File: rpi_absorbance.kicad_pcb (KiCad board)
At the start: 2 copper layers, 33 parts, among them CON1 BARREL_JACK, P1 CONN_02X04, P2 CONN_01X02, P3 RPI_HEADER, P4 STEPPER_CONN, P5 CONN_02X05, Q1 ZTX692B, U1 R-78B5.0-1.5L, U2 MUN5216DW1T1G, U3 DRV8825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

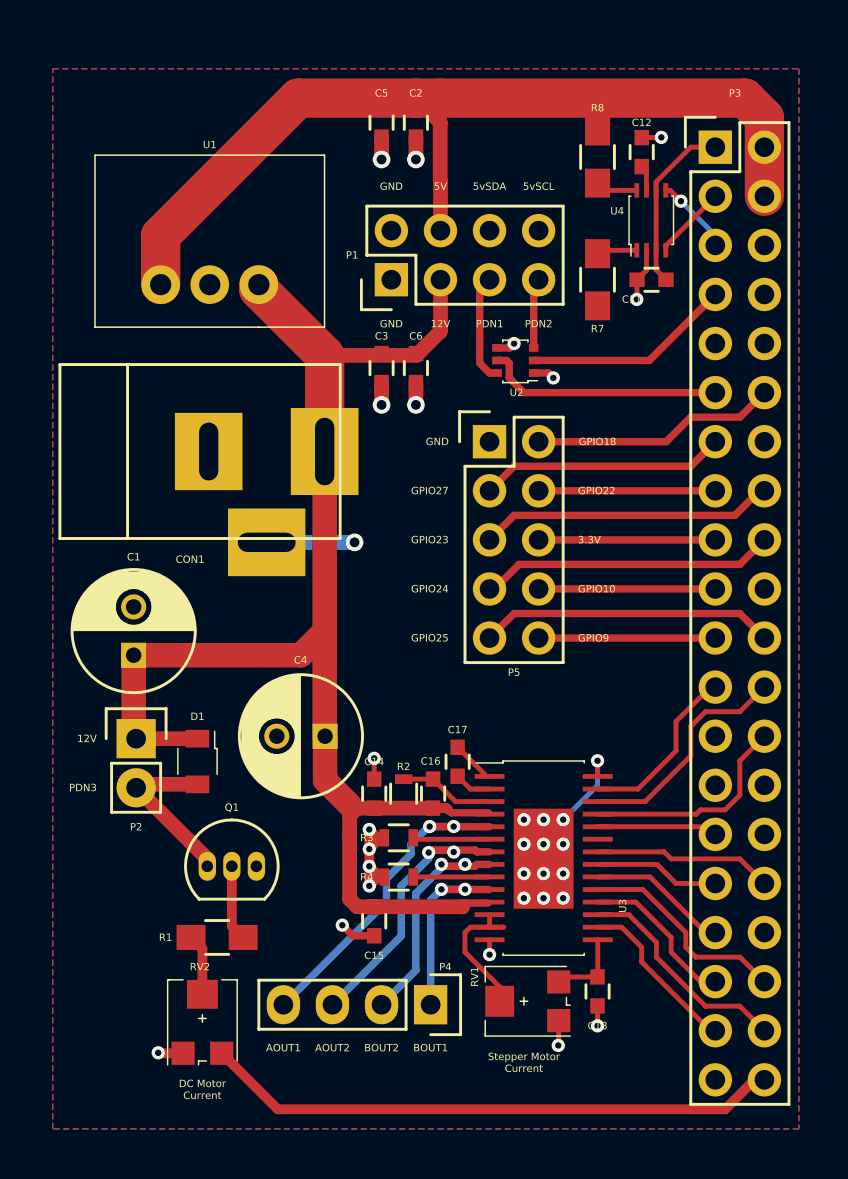
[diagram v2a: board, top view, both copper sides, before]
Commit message: Add missing connections
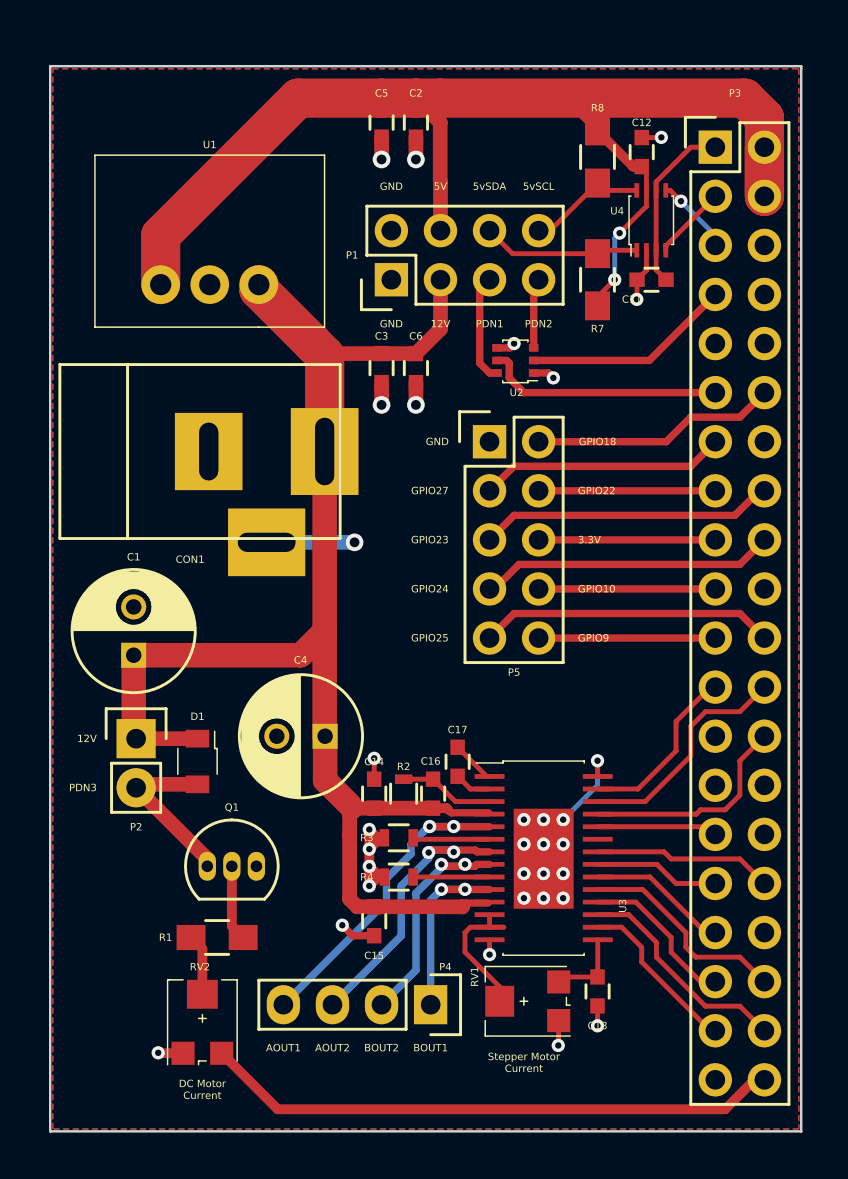
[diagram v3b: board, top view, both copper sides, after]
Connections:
- P3 pad 17: +3V3 -> /3.3v
- P5 pad 6: +3V3 -> /3.3v
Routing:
- net +5V: track 49.9 -> 73.7 mm, vias 0 -> 2
- net /3.3v: track 0.00 -> 9.14 mm
- net +3V3: track 18.2 -> 9.08 mm
- net /5vSDA: track 2.46 -> 8.54 mm
- net /5vSCL: track 1.66 -> 5.72 mm
- net +12V: track 75.4 -> 78.3 mm
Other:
- board outline added: 38.9 x 55.1 mm
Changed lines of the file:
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@@
 (kicad_pcb (version 4) (host pcbnew 4.0.2-4+6225~38~ubuntu14.04.1-stable)
   (general
-    (links 111)
-    (no_connects 43)
-    (area 145.288 90.932 184.055401 145.796001)
+    (links 110)
+    (no_connects 0)
+    (area 0 0 0 0)
     (thickness 1.6)
-    (drawings 26)
-    (tracks 357)
+    (drawings 31)
+    (tracks 383)
     (zones 0)
     (modules 33)
-    (nets 47)
+    (nets 48)
   )
   (page A4)
@@
   )
   (setup
-    (last_trace_width 2.032)
+    (last_trace_width 0.381)
     (user_trace_width 0.254)
     (user_trace_width 0.381)
@@
   (net 45 /GPIO27)
   (net 46 /GPIO22)
+  (net 47 /3.3v)
   (net_class Default "This is the default net class."
     (clearance 0.1524)
@@
     (add_net +3V3)
     (add_net +5V)
+    (add_net /3.3v)
     (add_net /3.3vSCL)
     (add_net /3.3vSDA)
@@
       (net 41 /GPIO23))
     (pad 17 thru_hole oval (at 0 20.32) (size 1.7272 1.7272) (drill 1.016) (layers *.Cu *.Mask F.SilkS)
-      (net 4 +3V3))
+      (net 47 /3.3v))
     (pad 18 thru_hole oval (at 2.54 20.32) (size 1.7272 1.7272) (drill 1.016) (layers *.Cu *.Mask F.SilkS)
       (net 42 /GPIO24))
@@
       (net 41 /GPIO23))
     (pad 6 thru_hole oval (at 2.54 5.08) (size 1.7272 1.7272) (drill 1.016) (layers *.Cu *.Mask F.SilkS)
-      (net 4 +3V3))
+      (net 47 /3.3v))
     (pad 7 thru_hole oval (at 0 7.62) (size 1.7272 1.7272) (drill 1.016) (layers *.Cu *.Mask F.SilkS)
       (net 42 /GPIO24))
@@
     )
   )
+  (gr_line (start 184.023 90.805) (end 184.023 90.932) (angle 90) (layer Edge.Cuts) (width 0.127))
+  (gr_line (start 145.161 90.805) (end 184.023 90.805) (angle 90) (layer Edge.Cuts) (width 0.127))
+  (gr_line (start 145.161 145.923) (end 145.161 90.805) (angle 90) (layer Edge.Cuts) (width 0.127))
+  (gr_line (start 184.023 145.923) (end 145.161 145.923) (angle 90) (layer Edge.Cuts) (width 0.127))
+  (gr_line (start 184.023 90.932) (end 184.023 145.923) (angle 90) (layer Edge.Cuts) (width 0.127))
   (gr_text PDN3 (at 147.574 128.143) (layer F.SilkS)
     (effects (font (size 0.381 0.381) (thickness 0.0762)) (justify right))
@@
     (effects (font (size 0.381 0.381) (thickness 0.0762)))
   )
+  (segment (start 161.925 129.1978) (end 163.449 129.1978) (width 0.381) (layer F.Cu) (net 1))
+  (segment (start 162.306 105.676) (end 159.27 105.676) (width 0.762) (layer F.Cu) (net 1))
+  (segment (start 158.75 105.918) (end 158.75 105.156) (width 0.762) (layer F.Cu) (net 1))
+  (segment (start 159.028 105.918) (end 158.75 105.918) (width 0.762) (layer F.Cu) (net 1))
+  (segment (start 159.27 105.676) (end 159.028 105.918) (width 0.762) (layer F.Cu) (net 1))
+  (segment (start 164.084 105.676) (end 162.306 105.676) (width 0.762) (layer F.Cu) (net 1))
+  (segment (start 165.354 101.854) (end 165.354 104.406) (width 0.762) (layer F.Cu) (net 1))
+  (segment (start 165.354 104.406) (end 164.084 105.676) (width 0.762) (layer F.Cu) (net 1))
   (segment (start 155.956 102.108) (end 155.956 102.362) (width 2.032) (layer F.Cu) (net 1))
-  (segment (start 155.956 102.362) (end 159.36214 105.76814) (width 2.032) (layer F.Cu) (net 1))
-  (segment (start 165.342 104.394) (end 165.342 104.533) (width 0.762) (layer F.Cu) (net 1))
-  (segment (start 165.342 104.533) (end 164.10686 105.76814) (width 0.762) (layer F.Cu) (net 1))
-  (segment (start 164.10686 105.76814) (end 159.36214 105.76814) (width 0.762) (layer F.Cu) (net 1))
-  (segment (start 165.354 101.854) (end 165.354 104.382) (width 0.762) (layer F.Cu) (net 1))
-  (segment (start 165.354 104.382) (end 165.342 104.394) (width 0.762) (layer F.Cu) (net 1))
+  (segment (start 155.956 102.362) (end 158.75 105.156) (width 2.032) (layer F.Cu) (net 1))
+  (segment (start 158.75 105.156) (end 159.36214 105.76814) (width 2.032) (layer F.Cu) (net 1))
+  (segment (start 159.36214 110.744) (end 159.36214 105.76814) (width 2.032) (layer F.Cu) (net 1))
   (segment (start 152.781 125.603) (end 149.606 125.603) (width 0.762) (layer F.Cu) (net 1))
   (segment (start 149.479 121.285) (end 149.479 125.476) (width 1.27) (layer F.Cu) (net 1))
@@
   (segment (start 159.385 110.76686) (end 159.36214 110.744) (width 1.27) (layer F.Cu) (net 1))
   (segment (start 159.385 110.76686) (end 159.36214 110.744) (width 0.762) (layer F.Cu) (net 1))
-  (segment (start 159.36214 110.744) (end 159.36214 105.76814) (width 2.032) (layer F.Cu) (net 1))
   (segment (start 167.8178 134.112) (end 166.6734 134.112) (width 0.381) (layer F.Cu) (net 1))
   (segment (start 166.6734 134.112) (end 166.4836 134.3018) (width 0.381) (layer F.Cu) (net 1))
@@
   (segment (start 171.7035 131.8138) (end 170.694 131.8138) (width 0.254) (layer F.Cu) (net 2))
   (segment (start 170.688 133.9088) (end 170.694 133.9028) (width 0.254) (layer F.Cu) (net 2))
+  (segment (start 182.118 94.996) (end 182.118 97.536) (width 2.032) (layer F.Cu) (net 3))
+  (segment (start 176.014 97.23) (end 176.014 98.052) (width 0.254) (layer F.Cu) (net 3))
+  (segment (start 174.371 101.854) (end 173.482 102.743) (width 0.254) (layer F.Cu) (net 3))
+  (via (at 174.371 101.854) (size 0.6858) (drill 0.3302) (layers F.Cu B.Cu) (net 3))
+  (segment (start 174.371 99.695) (end 174.371 101.854) (width 0.254) (layer B.Cu) (net 3))
+  (segment (start 174.625 99.441) (end 174.371 99.695) (width 0.254) (layer B.Cu) (net 3))
+  (via (at 174.625 99.441) (size 0.6858) (drill 0.3302) (layers F.Cu B.Cu) (net 3))
+  (segment (start 176.014 98.052) (end 174.625 99.441) (width 0.254) (layer F.Cu) (net 3))
+  (segment (start 173.482 102.743) (end 173.482 103.204) (width 0.254) (layer F.Cu) (net 3))
+  (segment (start 175.328 96) (end 173.482 94.154) (width 0.508) (layer F.Cu) (net 3))
+  (segment (start 175.768 96) (end 175.328 96) (width 0.508) (layer F.Cu) (net 3))
+  (segment (start 164.084 92.976) (end 172.304 92.976) (width 0.381) (layer F.Cu) (net 3))
+  (segment (start 172.304 92.976) (end 173.482 94.154) (width 0.381) (layer F.Cu) (net 3))
+  (segment (start 164.084 92.976) (end 164.084 92.456) (width 0.381) (layer F.Cu) (net 3))
+  (segment (start 162.306 92.976) (end 162.306 92.456) (width 0.381) (layer F.Cu) (net 3))
+  (segment (start 162.306 92.456) (end 162.306 92.329) (width 0.381) (layer F.Cu) (net 3))
+  (segment (start 162.306 92.329) (end 162.306 92.456) (width 0.381) (layer F.Cu) (net 3))
   (segment (start 150.876 102.108) (end 150.876 99.568) (width 2.032) (layer F.Cu) (net 3))
-  (segment (start 157.988 92.456) (end 164.084 92.456) (width 2.032) (layer F.Cu) (net 3))
+  (segment (start 157.988 92.456) (end 162.306 92.456) (width 2.032) (layer F.Cu) (net 3))
+  (segment (start 162.306 92.456) (end 164.084 92.456) (width 2.032) (layer F.Cu) (net 3))
   (segment (start 150.876 99.568) (end 157.988 92.456) (width 2.032) (layer F.Cu) (net 3))
   (segment (start 165.342 96.774) (end 165.342 93.714) (width 0.762) (layer F.Cu) (net 3))
@@
   (segment (start 176.014 96.246) (end 175.768 96) (width 0.254) (layer F.Cu) (net 3))
   (segment (start 176.014 95.762) (end 176.01 95.758) (width 0.254) (layer F.Cu) (net 3))
-  (segment (start 179.578 115.316) (end 170.434 115.316) (width 0.381) (layer F.Cu) (net 4))
   (segment (start 176.514 97.23) (end 176.514 100.33) (width 0.254) (layer F.Cu) (net 4))
   (segment (start 176.514 100.33) (end 176.514 101.342) (width 0.254) (layer F.Cu) (net 4))
@@
   (segment (start 173.494 136.0088) (end 173.494 137.922) (width 0.254) (layer F.Cu) (net 8))
   (segment (start 173.494 137.922) (end 173.482 137.934) (width 0.254) (layer F.Cu) (net 8))
+  (segment (start 173.482 100.504) (end 169.084 100.504) (width 0.254) (layer F.Cu) (net 9))
+  (segment (start 169.084 100.504) (end 167.894 99.314) (width 0.254) (layer F.Cu) (net 9))
   (segment (start 175.514 100.33) (end 173.656 100.33) (width 0.254) (layer F.Cu) (net 9))
   (segment (start 173.656 100.33) (end 173.402 100.584) (width 0.254) (layer F.Cu) (net 9))
   (segment (start 173.656 100.33) (end 173.482 100.504) (width 0.254) (layer F.Cu) (net 9))
+  (segment (start 170.434 99.314) (end 171.022 99.314) (width 0.254) (layer F.Cu) (net 10))
+  (segment (start 171.022 99.314) (end 173.482 96.854) (width 0.254) (layer F.Cu) (net 10))
   (segment (start 175.514 97.23) (end 173.858 97.23) (width 0.254) (layer F.Cu) (net 10))
   (segment (start 177.014 100.33) (end 177.014 100.1) (width 0.254) (layer F.Cu) (net 11))
@@
   (segment (start 178.308 111.506) (end 169.164 111.506) (width 0.381) (layer F.Cu) (net 45))
   (segment (start 179.578 112.776) (end 170.434 112.776) (width 0.381) (layer F.Cu) (net 46))
+  (segment (start 179.578 115.316) (end 170.434 115.316) (width 0.381) (layer F.Cu) (net 47))
   (zone (net 2) (net_name GND) (layer F.Cu) (hatch edge 0.508)
     (connect_pads yes (clearance 0.254))
     (min_thickness 0.254)
-    (fill (arc_segments 16) (thermal_gap 0.508) (thermal_bridge_width 0.508))
+    (fill yes (arc_segments 16) (thermal_gap 0.508) (thermal_bridge_width 0.508))
     (polygon
       (pts
@@
     (connect_pads yes (clearance 0.254))
     (min_thickness 0.254)
-    (fill (arc_segments 16) (thermal_gap 0.508) (thermal_bridge_width 0.508))
+    (fill yes (arc_segments 16) (thermal_gap 0.508) (thermal_bridge_width 0.508))
     (polygon
       (pts

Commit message: Replace power input footprint
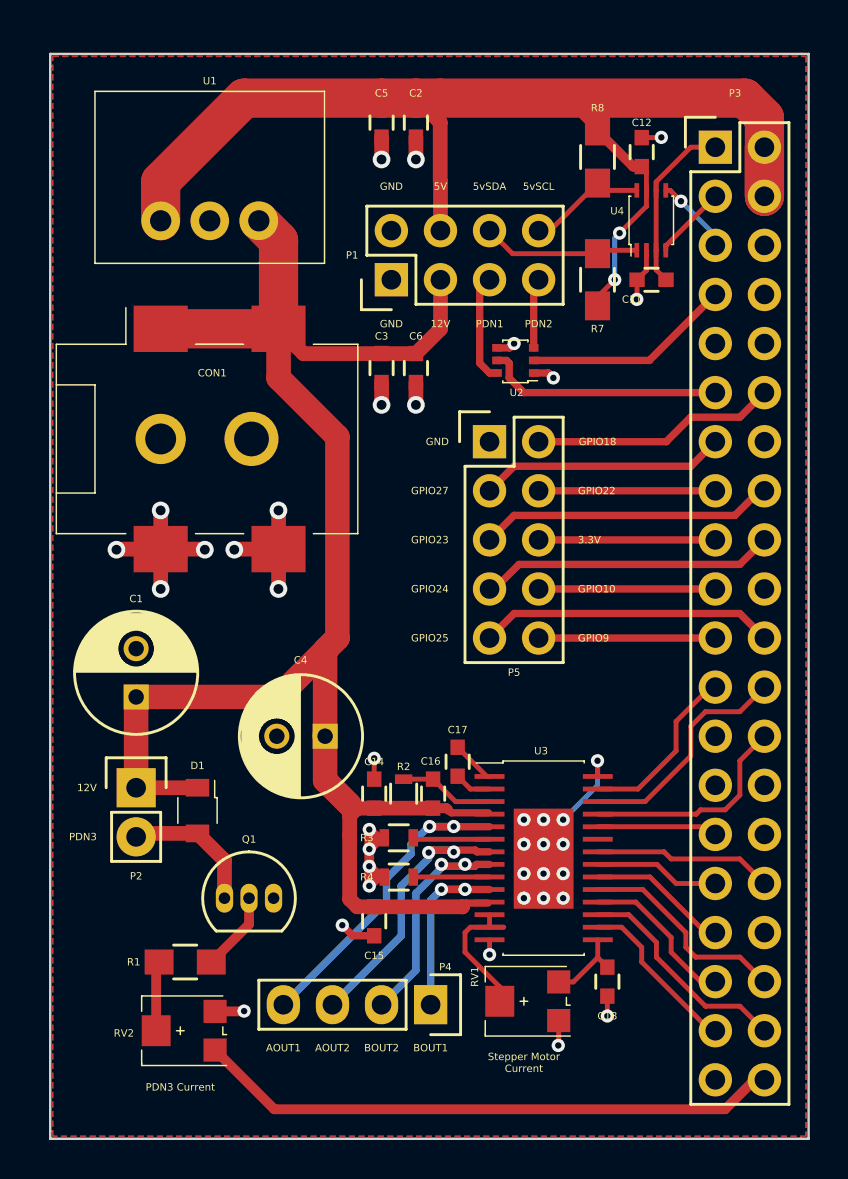
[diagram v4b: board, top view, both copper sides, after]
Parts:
- CON1: footprint footprints:CUI_BARREL_JACK -> footprints:CUI_PJ-002AH-SMT
- moved CON1 6.75 mm to (150.9, 104.4)
- moved U1 3.30 mm to (156.0, 98.8)
- moved D1 2.54 mm to (152.8, 128.1)
- moved P2 2.54 mm to (149.6, 128.1)
- moved C1 2.16 mm to (149.6, 123.4)
- moved R1 2.08 mm to (152.1, 137.2)
- moved Q1 1.88 mm to (154.2, 133.9)
- moved RV2 1.31 mm to (151.9, 140.7), turned to 90 degrees
- moved C18 0.72 mm to (174.0, 138.2)
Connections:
- RV2 pad 1: GND -> /PERI
- RV2 pad 3: /PERI -> GND
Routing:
- net +12V: track 78.3 -> 91.4 mm
- net GND: track 71.3 -> 82.0 mm, vias 32 -> 38
- net +5V: track 73.7 -> 72.0 mm
- net Net-(D1-Pad2): track 8.84 -> 7.18 mm
- net /V3P3: track 4.05 -> 4.55 mm
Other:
- board size 38.9 x 55.1 mm -> 39.2 x 56.1 mm
- board text added: "PDN3 Current"
- board text removed: "DC Motor Current"

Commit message: Reorganize pcb
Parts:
- P5: value CONN_02X05 -> CONN_02X06; footprint Pin_Headers:Pin_Header_Straight_2x05 -> Pin_Headers:Pin_Header_Straight_2x06
- U2: value MUN5216DW1T1G -> NXP_PUMH10
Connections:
- net /LED1 renamed /PDN1
- net /LED2 renamed /PDN2
- net /PERI renamed /PDN3
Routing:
- net +5V: track 72.0 -> 97.7 mm
- net GND: track 82.0 -> 84.7 mm, vias 38 -> 39
- net +12V: track 91.4 -> 93.0 mm
